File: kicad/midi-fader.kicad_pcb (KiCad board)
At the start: 2 copper layers, 73.7 x 78.7 mm, 163 parts, among them J1 SWD, J2 EXTERNAL_OUT, J3 EXTERNAL_IN, J4 USB_OTG, SW1 TR2-21-L5, SW2 TR2-21-L5, U1 STM32F042KxT, U2 USBLC6-2, U3 MCP1603, U4 MIC2776L, U5 MIC5501-XYM5, U6 74HC165, U7 STP08DP05

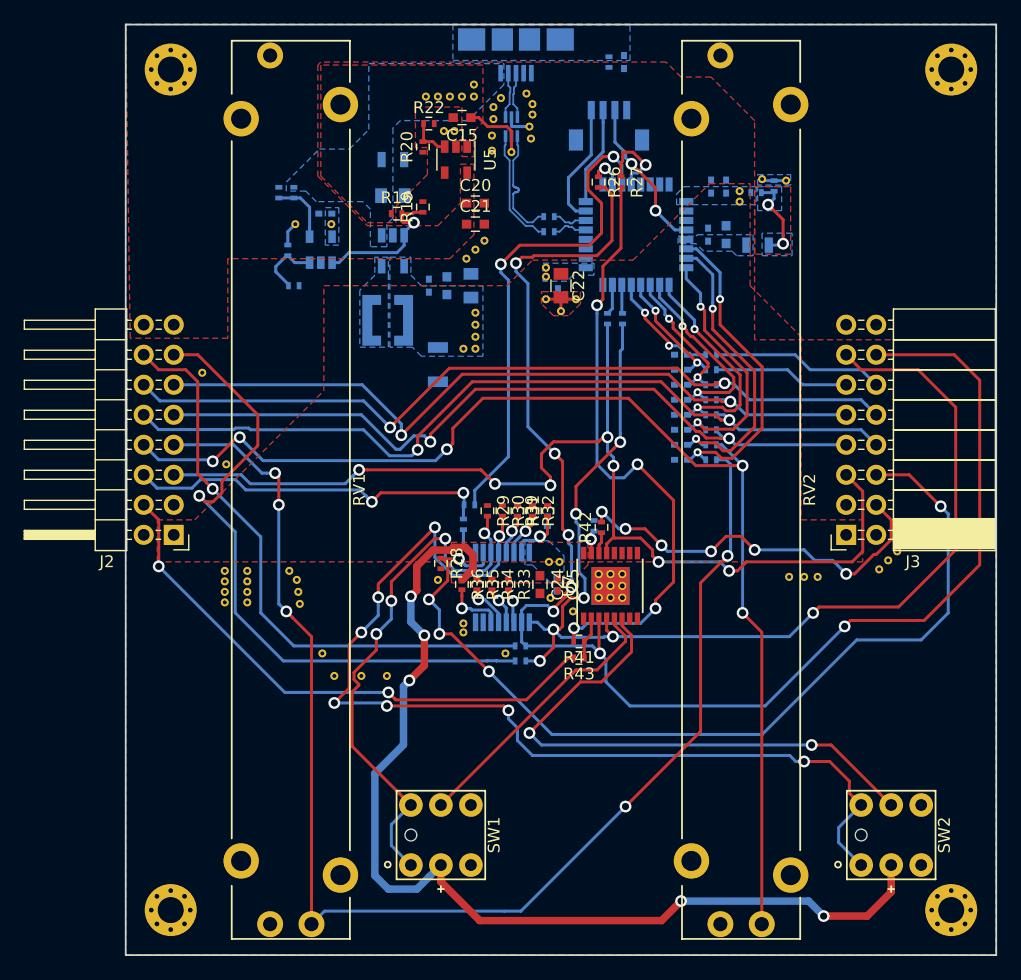
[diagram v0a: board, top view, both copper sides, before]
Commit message: Added stub-removal resistors on clock lines, started cleaning silkscreen
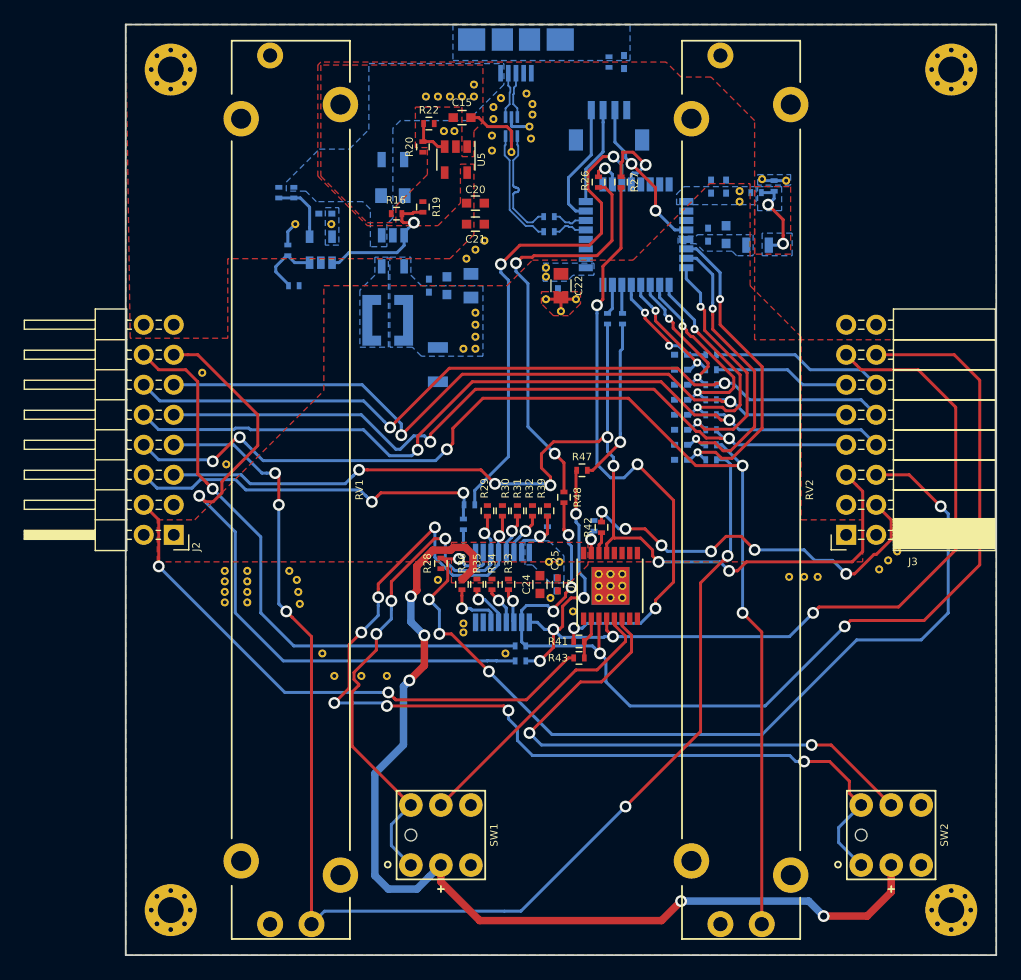
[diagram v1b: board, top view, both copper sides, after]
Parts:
- added R47: 0, Resistors_SMD:R_0402, F.Cu at (155.4, 101.2)
- added R48: 0, Resistors_SMD:R_0402, F.Cu at (153.9, 103.5)
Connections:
- J3 pad 13: /Digital Control/LCLK -> /Input/LCLK_LCL
- J3 pad 14: /Digital Control/SCLK -> /Input/SCLK_LCL
- R45 pad 1: /Digital Control/SCLK -> /Input/SCLK_LCL
- R46 pad 2: /Digital Control/LCLK -> /Input/LCLK_LCL
- U6 pad 1: /Digital Control/LCLK -> /Input/LCLK_LCL
- U6 pad 2: /Digital Control/SCLK -> /Input/SCLK_LCL
- U7 pad 3: /Digital Control/SCLK -> /Input/SCLK_LCL
- U7 pad 4: /Digital Control/LCLK -> /Input/LCLK_LCL
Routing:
- net /Digital Control/SCLK: track 127.3 -> 35.3 mm, vias 7 -> 2
- net /Input/SCLK_LCL: track 0.00 -> 91.1 mm, vias 0 -> 5
- net /Digital Control/LCLK: track 98.8 -> 13.9 mm, vias 7 -> 1
- net /Input/LCLK_LCL: track 0.00 -> 84.8 mm, vias 0 -> 6

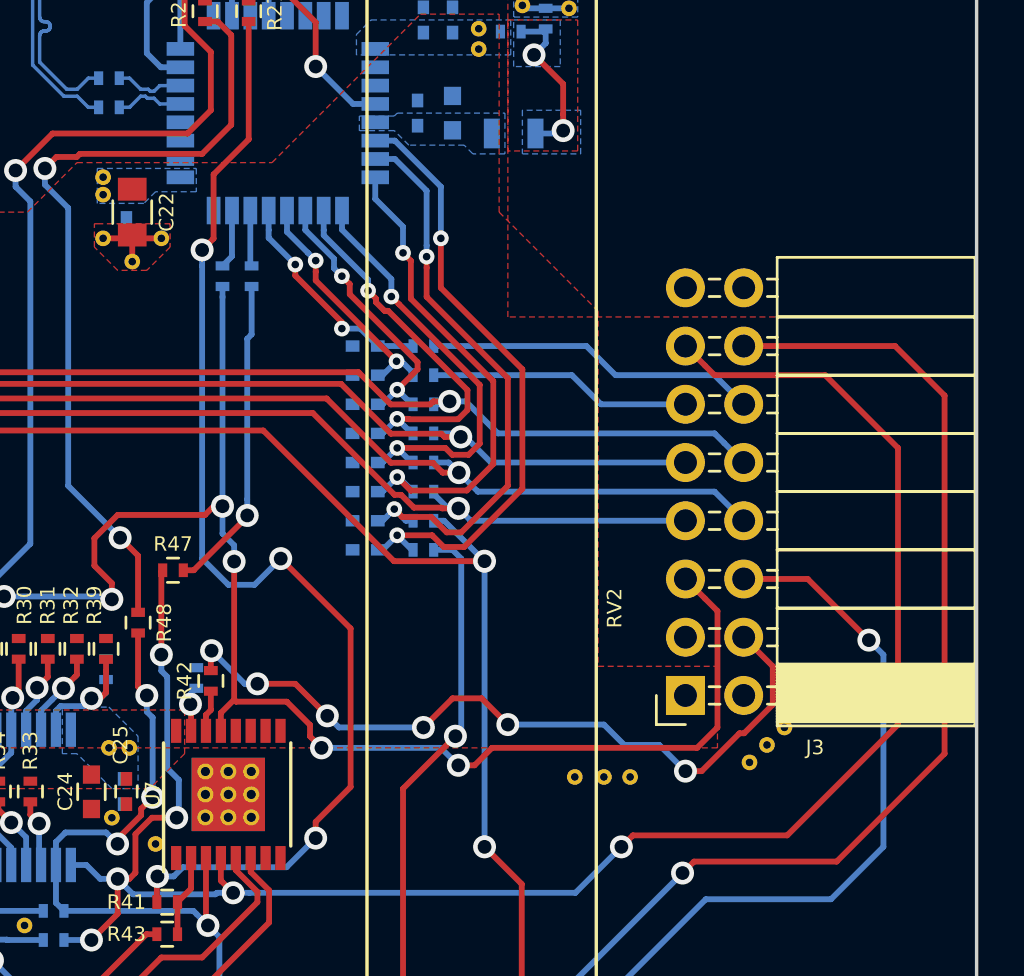
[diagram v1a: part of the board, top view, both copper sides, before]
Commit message: Finished refdes tweaks, added OSHW logo and license
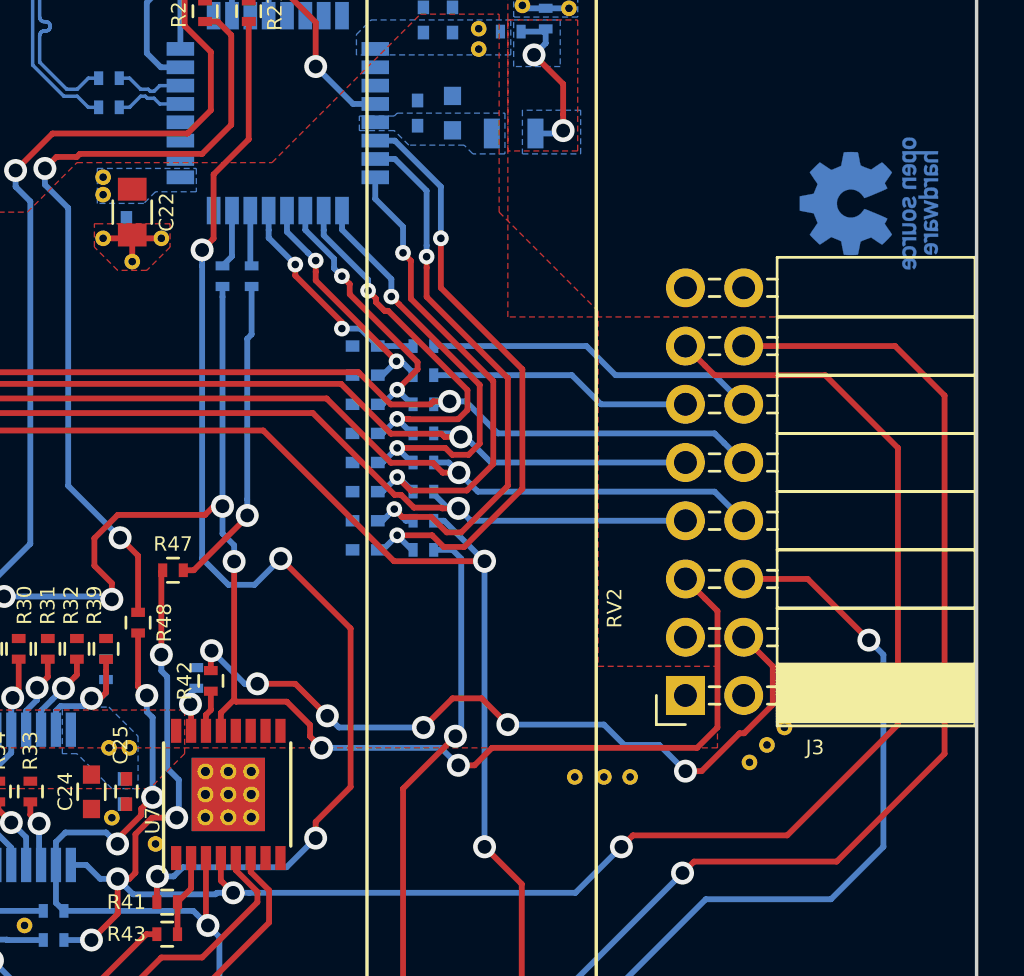
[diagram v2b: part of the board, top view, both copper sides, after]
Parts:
- added REF***: OSHW-Logo_5.7x6mm_SilkScreen, Symbols:OSHW-Logo_5.7x6mm_SilkScreen, B.Cu at (185.8, 85.2)
- added REF***: OSHW-Logo_5.7x6mm_Copper, Symbols:OSHW-Logo_5.7x6mm_Copper, B.Cu at (185.8, 85.2)
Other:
- board text added: "Kevin Cuzner"
- board text added: "Rev A 2018"
- board text added: "USB Midi-Fader"
- board text added: "http://kevincuzner.com/"

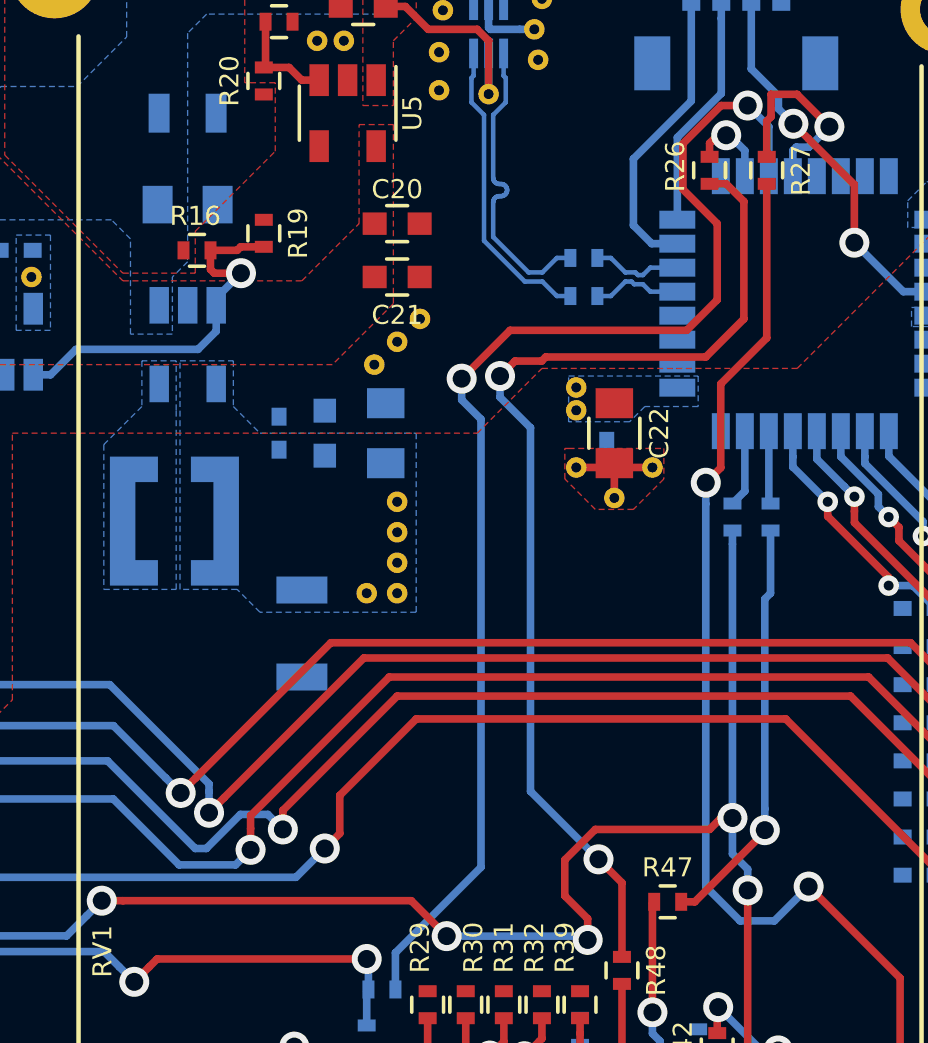
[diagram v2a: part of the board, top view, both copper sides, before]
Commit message: Moved sense location of VDD
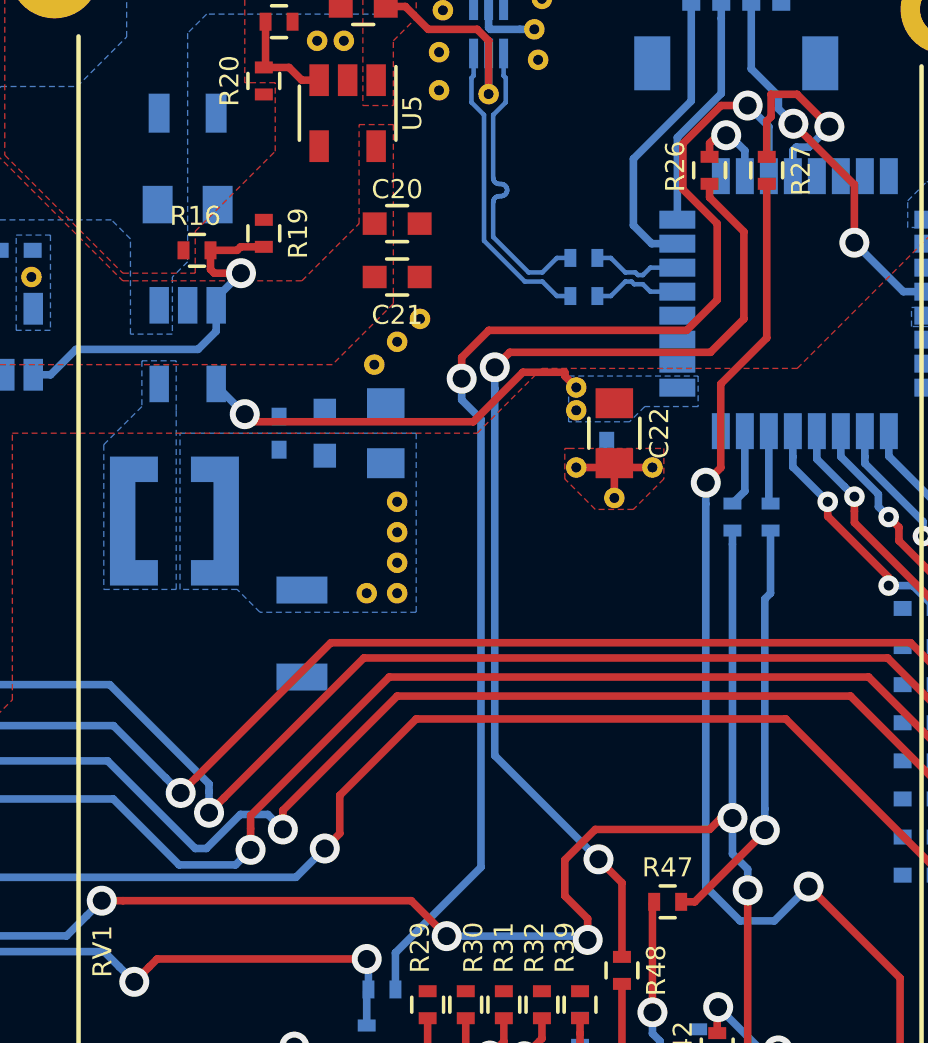
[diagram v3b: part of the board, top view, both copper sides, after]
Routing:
- net VDD: track 88.9 -> 102.4 mm, vias 5 -> 6
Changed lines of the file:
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@@
 (kicad_pcb (version 4) (host pcbnew 4.0.7)
   (general
-    (links 0)
+    (links 333)
     (no_connects 0)
-    (area 116.764999 63.424999 190.575001 142.315001)
+    (area 107.626599 48.1 211.05 142.6574)
     (thickness 1.6)
     (drawings 13)
-    (tracks 963)
+    (tracks 970)
     (zones 0)
     (modules 167)
@@
   (gr_line (start 190.5 63.5) (end 190.5 142.24) (layer Edge.Cuts) (width 0.15))
   (gr_line (start 116.84 63.5) (end 190.5 63.5) (layer Edge.Cuts) (width 0.15))
+  (segment (start 141.351 84.963) (end 141.605 85.217) (width 0.254) (layer F.Cu) (net 1))
+  (segment (start 141.605 85.217) (end 148.971 85.217) (width 0.254) (layer F.Cu) (net 1))
+  (segment (start 148.971 85.217) (end 150.622 83.566) (width 0.254) (layer F.Cu) (net 1))
+  (segment (start 150.622 83.566) (end 152.019 83.566) (width 0.254) (layer F.Cu) (net 1))
+  (segment (start 152.019 83.566) (end 152.019 83.693) (width 0.254) (layer F.Cu) (net 1))
+  (segment (start 152.019 83.693) (end 152.4 84.074) (width 0.254) (layer F.Cu) (net 1))
+  (segment (start 140.398184 83.955402) (end 140.398184 84.010184) (width 0.254) (layer B.Cu) (net 1))
+  (segment (start 140.398184 84.010184) (end 141.351 84.963) (width 0.254) (layer B.Cu) (net 1))
+  (via (at 141.351 84.963) (size 1) (drill 0.6) (layers F.Cu B.Cu) (net 1))
   (segment (start 145.288 110.421) (end 145.388 110.421) (width 0.635) (layer F.Cu) (net 1))
   (segment (start 145.388 110.421) (end 146.223 109.586) (width 0.635) (layer F.Cu) (net 1))
@@
   (segment (start 158.877 88.842) (end 158.877 90.932) (width 0.254) (layer B.Cu) (net 56))
   (segment (start 158.877 90.932) (end 158.686037 91.122963) (width 0.254) (layer B.Cu) (net 56))
+  (segment (start 149.68413 84.108722) (end 149.68413 83.401616) (width 0.254) (layer B.Cu) (net 57))
+  (segment (start 150.184129 82.901617) (end 149.68413 83.401616) (width 0.254) (layer F.Cu) (net 57))
+  (segment (start 157.988 81.788) (end 156.874383 82.901617) (width 0.254) (layer F.Cu) (net 57))
+  (segment (start 157.988 78.882) (end 157.988 81.788) (width 0.254) (layer F.Cu) (net 57))
+  (segment (start 156.874383 82.901617) (end 150.184129 82.901617) (width 0.254) (layer F.Cu) (net 57))
+  (via (at 149.68413 83.401616) (size 1) (drill 0.6) (layers F.Cu B.Cu) (net 57))
+  (segment (start 153.141627 99.801627) (end 149.68413 96.34413) (width 0.254) (layer B.Cu) (net 57))
+  (segment (start 149.68413 96.34413) (end 149.68413 84.108722) (width 0.254) (layer B.Cu) (net 57))
+  (segment (start 156.845 77.285) (end 156.845 77.739) (width 0.254) (layer F.Cu) (net 57))
+  (segment (start 156.845 77.739) (end 157.988 78.882) (width 0.254) (layer F.Cu) (net 57))
   (segment (start 153.924 103.055) (end 153.924 100.584) (width 0.254) (layer F.Cu) (net 57))
   (via (at 153.141627 99.801627) (size 1) (drill 0.6) (layers F.Cu B.Cu) (net 57))
   (segment (start 153.924 100.584) (end 153.141627 99.801627) (width 0.254) (layer F.Cu) (net 57))
-  (segment (start 149.86 83.693) (end 150.359999 83.193001) (width 0.254) (layer F.Cu) (net 57))
-  (segment (start 157.988 81.788) (end 157.988 77.874) (width 0.254) (layer F.Cu) (net 57))
-  (segment (start 157.988 77.874) (end 157.399 77.285) (width 0.254) (layer F.Cu) (net 57))
-  (segment (start 150.359999 83.193001) (end 151.248999 83.193001) (width 0.254) (layer F.Cu) (net 57))
-  (segment (start 151.248999 83.193001) (end 151.384 83.058) (width 0.254) (layer F.Cu) (net 57))
-  (segment (start 151.384 83.058) (end 156.718 83.058) (width 0.254) (layer F.Cu) (net 57))
-  (segment (start 156.718 83.058) (end 157.988 81.788) (width 0.254) (layer F.Cu) (net 57))
-  (segment (start 157.399 77.285) (end 156.845 77.285) (width 0.254) (layer F.Cu) (net 57))
-  (segment (start 153.141627 99.801627) (end 150.876 97.536) (width 0.254) (layer B.Cu) (net 57))
-  (segment (start 150.876 97.536) (end 150.876 85.416106) (width 0.254) (layer B.Cu) (net 57))
-  (segment (start 150.876 85.416106) (end 149.86 84.400106) (width 0.254) (layer B.Cu) (net 57))
-  (segment (start 149.86 84.400106) (end 149.86 83.693) (width 0.254) (layer B.Cu) (net 57))
-  (via (at 149.86 83.693) (size 1) (drill 0.6) (layers F.Cu B.Cu) (net 57))
   (segment (start 158.82 85.53) (end 158.82 87.885) (width 0.254) (layer B.Cu) (net 58))
   (segment (start 158.82 87.885) (end 158.877 87.942) (width 0.254) (layer B.Cu) (net 58))
@@
   (segment (start 145.288 112.903) (end 145.288 111.829) (width 0.254) (layer F.Cu) (net 70))
   (via (at 145.288 112.903) (size 1) (drill 0.6) (layers F.Cu B.Cu) (net 70))
-  (segment (start 158.115 74.676) (end 157.226 74.676) (width 0.254) (layer F.Cu) (net 71))
-  (segment (start 157.226 74.676) (end 155.956 75.946) (width 0.254) (layer F.Cu) (net 71))
+  (segment (start 149.486187 82.169) (end 148.581247 83.07394) (width 0.254) (layer F.Cu) (net 71))
+  (segment (start 156.083 82.169) (end 149.486187 82.169) (width 0.254) (layer F.Cu) (net 71))
   (segment (start 155.956 75.946) (end 155.956 77.47) (width 0.254) (layer F.Cu) (net 71))
+  (segment (start 157.226 74.676) (end 155.956 75.946) (width 0.254) (layer F.Cu) (net 71))
   (segment (start 155.956 77.47) (end 157.099 78.613) (width 0.254) (layer F.Cu) (net 71))
-  (segment (start 157.099 78.613) (end 157.099 81.153) (width 0.254) (layer F.Cu) (net 71))
   (segment (start 157.099 81.153) (end 156.083 82.169) (width 0.254) (layer F.Cu) (net 71))
-  (segment (start 156.083 82.169) (end 150.193293 82.169) (width 0.254) (layer F.Cu) (net 71))
-  (segment (start 150.193293 82.169) (end 148.581247 83.781046) (width 0.254) (layer F.Cu) (net 71))
+  (segment (start 148.581247 83.07394) (end 148.581247 83.781046) (width 0.254) (layer F.Cu) (net 71))
+  (segment (start 158.115 74.676) (end 157.226 74.676) (width 0.254) (layer F.Cu) (net 71))
+  (segment (start 157.099 78.613) (end 157.099 81.153) (width 0.254) (layer F.Cu) (net 71))
   (segment (start 146.373 104.14) (end 146.373 102.917486) (width 0.254) (layer B.Cu) (net 71))
   (segment (start 146.373 102.917486) (end 149.225 100.065486) (width 0.254) (layer B.Cu) (net 71))
@@
     (polygon
       (pts
-        (xy 140.97 83.185) (xy 140.97 84.709) (xy 141.859 85.598) (xy 147.066 85.598) (xy 147.066 91.567)
-        (xy 141.859 91.567) (xy 141.097 90.805) (xy 139.192 90.805) (xy 139.192 83.185)
+        (xy 147.066 85.598) (xy 147.066 91.567) (xy 141.859 91.567) (xy 141.097 90.805) (xy 139.192 90.805)
+        (xy 139.192 85.598)
       )
     )
